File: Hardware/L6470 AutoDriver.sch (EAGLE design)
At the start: 39 parts, among them U1 L6470

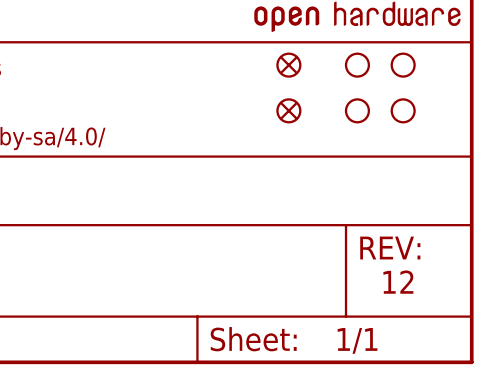
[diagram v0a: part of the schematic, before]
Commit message: Fixed BSilk to match TSilk, advanced version number
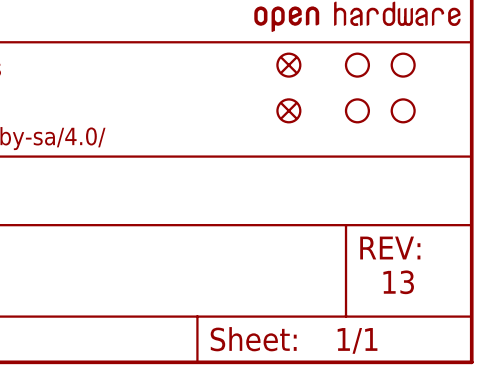
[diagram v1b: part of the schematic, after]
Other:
- note added: "13"
- note removed: "12"
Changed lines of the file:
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@@
 Motor supply must be enabled
 for chip comms to work!</text>
-<text x="238.76" y="7.62" size="2.54" layer="94">12</text>
+<text x="238.76" y="7.62" size="2.54" layer="94">13</text>
 <text x="76.2" y="167.64" size="1.778" layer="97">SJ3 allows you to route the SDO (serial
 data out) either to the next board (if this
